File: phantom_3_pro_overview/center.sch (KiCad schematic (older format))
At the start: 0 parts

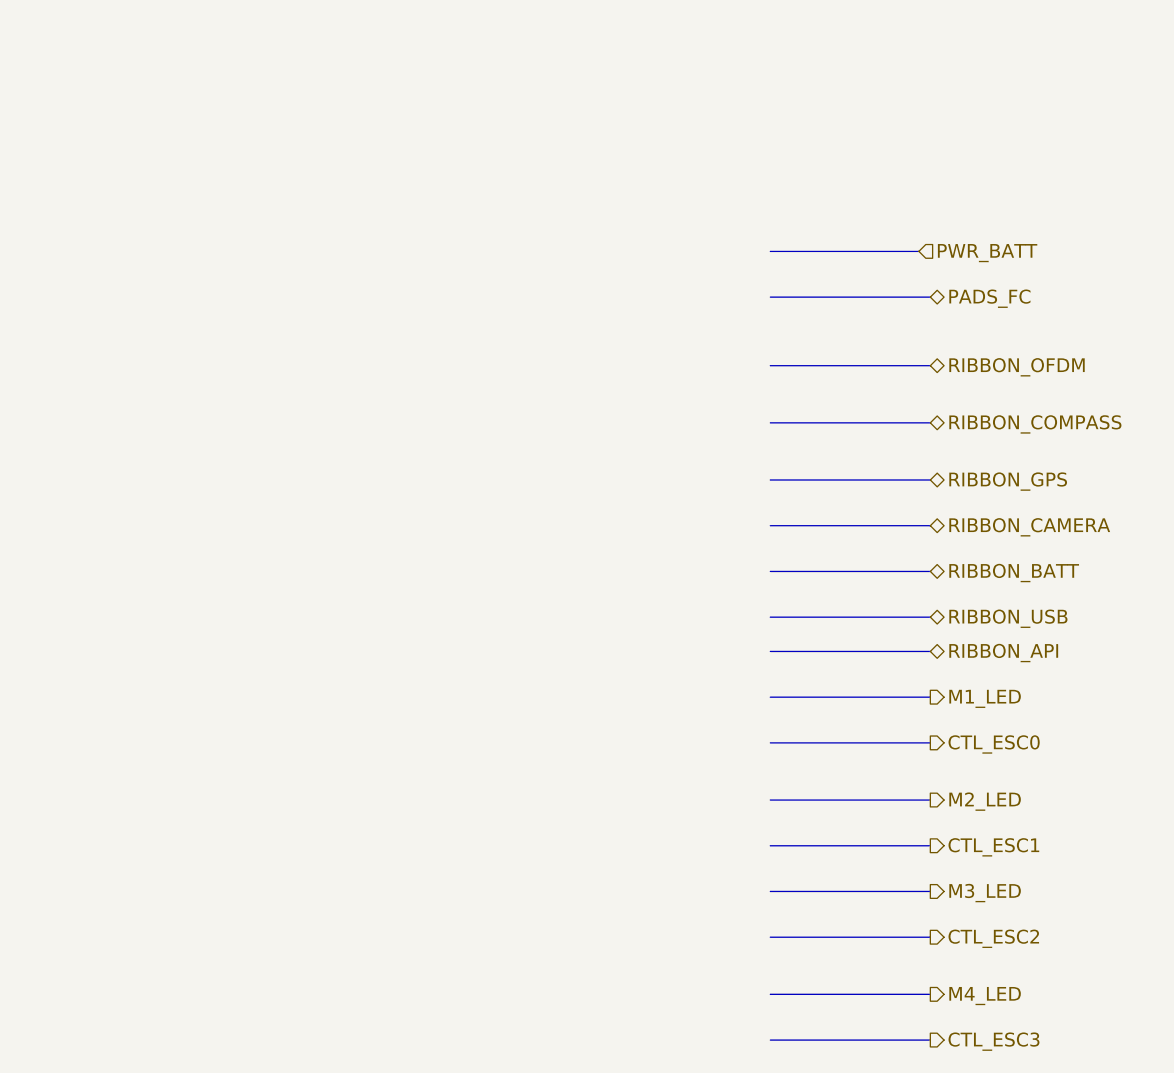
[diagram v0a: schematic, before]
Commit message: Overview: Conceptual schematics of some components.
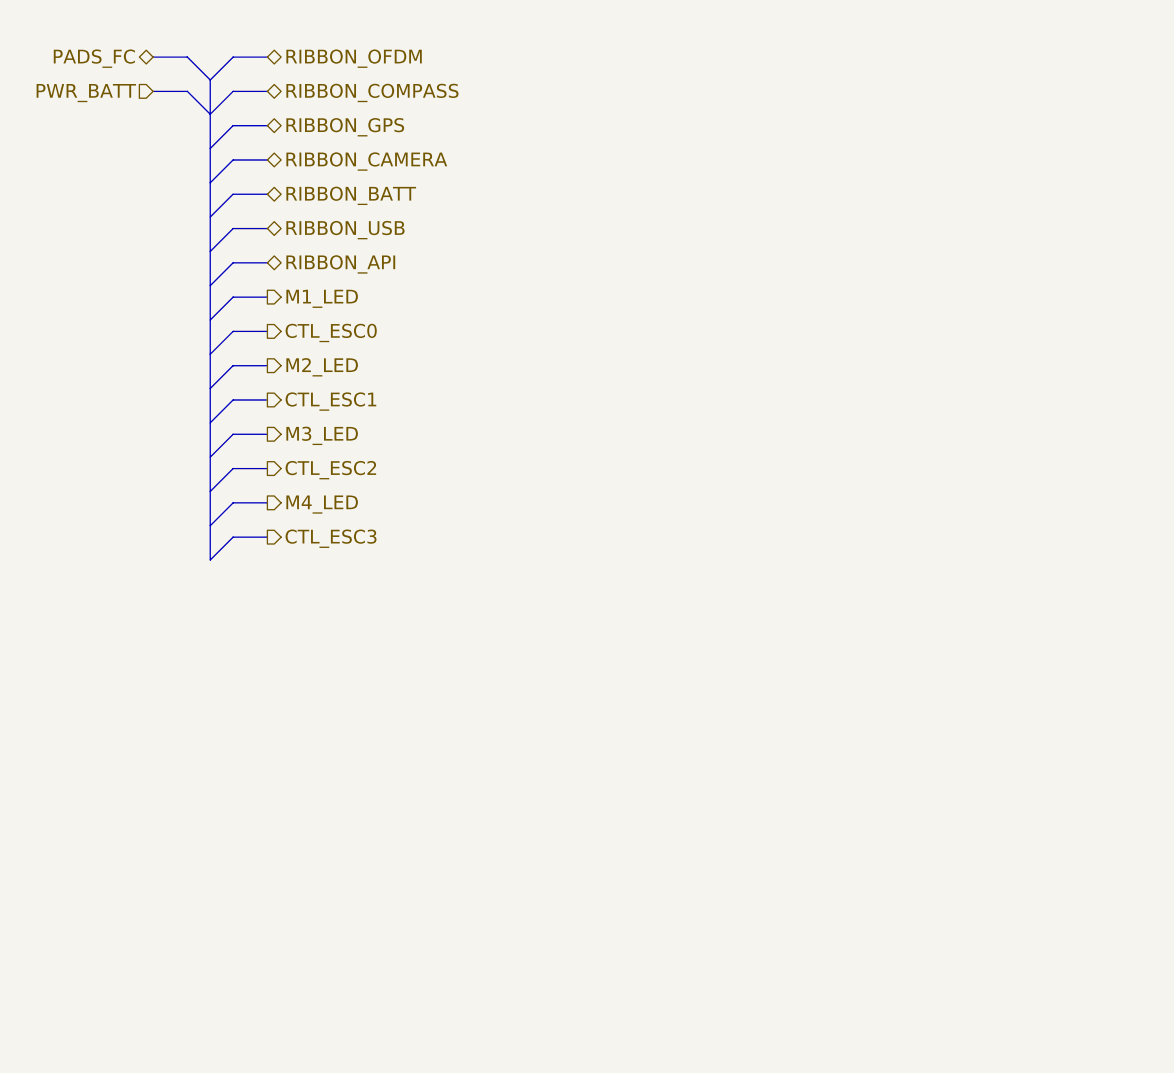
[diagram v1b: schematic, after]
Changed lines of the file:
@@
 LIBS:valves
 LIBS:motors
+LIBS:ic_dil_generic
+LIBS:sensors
+LIBS:u-blox
+LIBS:amplifiers
 LIBS:phantom_3_pro_overview-cache
 EELAYER 25 0
 EELAYER END
-$Descr A4 11693 8268
+$Descr User 5354 4725
 encoding utf-8
-Sheet 18 23
-Title ""
+Sheet 14 23
+Title "Overview of the Phantom 3 Pro Center part of MB"
 Date ""
 Rev ""
 Comp ""
-Comment1 ""
+Comment1 "This schematic does not aim to be electrically correct, it is conceptual."
 Comment2 ""
 Comment3 ""
 Comment4 ""
 $EndDescr
+Text HLabel 1050 700  0    60   BiDi ~ 0
+PADS_FC
+Text HLabel 1550 700  2    60   BiDi ~ 0
+RIBBON_OFDM
+Text HLabel 1550 850  2    60   BiDi ~ 0
+RIBBON_COMPASS
+Text HLabel 1550 1000 2    60   BiDi ~ 0
+RIBBON_GPS
+Text HLabel 1550 1150 2    60   BiDi ~ 0
+RIBBON_CAMERA
+Text HLabel 1550 1300 2    60   BiDi ~ 0
+RIBBON_BATT
+Text HLabel 1550 1450 2    60   BiDi ~ 0
+RIBBON_USB
+Text HLabel 1550 1600 2    60   BiDi ~ 0
+RIBBON_API
+Text HLabel 1550 1750 2    60   Output ~ 0
+M1_LED
+Text HLabel 1550 1900 2    60   Output ~ 0
+CTL_ESC0
+Text HLabel 1050 850  0    60   Input ~ 0
+PWR_BATT
+Text HLabel 1550 2050 2    60   Output ~ 0
+M2_LED
+Text HLabel 1550 2200 2    60   Output ~ 0
+CTL_ESC1
+Text HLabel 1550 2350 2    60   Output ~ 0
+M3_LED
+Text HLabel 1550 2500 2    60   Output ~ 0
+CTL_ESC2
+Text HLabel 1550 2650 2    60   Output ~ 0
+M4_LED
+Text HLabel 1550 2800 2    60   Output ~ 0
+CTL_ESC3
+Entry Bus Bus
+	1200 700  1300 800
 Wire Bus Line
-	3750 1750 4450 1750
-Text HLabel 4450 1750 2    60   BiDi ~ 0
-PADS_FC
+	1050 700  1200 700
 Wire Bus Line
-	3750 2050 4450 2050
+	1050 850  1200 850
+Entry Bus Bus
+	1200 850  1300 950
+Entry Bus Bus
+	1300 800  1400 700
+Entry Bus Bus
+	1300 950  1400 850
 Wire Bus Line
-	3750 2300 4450 2300
+	1400 700  1550 700
 Wire Bus Line
-	3750 2550 4450 2550
-Text HLabel 4450 2050 2    60   BiDi ~ 0
-RIBBON_OFDM
-Text HLabel 4450 2300 2    60   BiDi ~ 0
-RIBBON_COMPASS
-Text HLabel 4450 2550 2    60   BiDi ~ 0
-RIBBON_GPS
+	1400 850  1550 850
+Entry Bus Bus
+	1300 1100 1400 1000
+Entry Bus Bus
+	1300 1250 1400 1150
 Wire Bus Line
-	3750 2750 4450 2750
+	1400 1000 1550 1000
 Wire Bus Line
-	3750 2950 4450 2950
+	1400 1150 1550 1150
+Entry Bus Bus
+	1300 1400 1400 1300
+Entry Bus Bus
+	1300 1550 1400 1450
 Wire Bus Line
-	3750 3150 4450 3150
-Text HLabel 4450 2750 2    60   BiDi ~ 0
-RIBBON_CAMERA
-Text HLabel 4450 2950 2    60   BiDi ~ 0
-RIBBON_BATT
+	1400 1300 1550 1300
 Wire Bus Line
-	3750 3300 4450 3300
+	1400 1450 1550 1450
+Entry Bus Bus
+	1300 1700 1400 1600
+Entry Bus Bus
+	1300 1850 1400 1750
 Wire Bus Line
-	3750 3500 4450 3500
+	1400 1600 1550 1600
 Wire Bus Line
-	3750 3700 4450 3700
-Text HLabel 4450 3150 2    60   BiDi ~ 0
-RIBBON_USB
-Text HLabel 4450 3300 2    60   BiDi ~ 0
-RIBBON_API
-Text HLabel 4450 3500 2    60   Output ~ 0
-M1_LED
-Text HLabel 4450 3700 2    60   Output ~ 0
-CTL_ESC0
+	1400 1750 1550 1750
+Entry Bus Bus
+	1300 2000 1400 1900
+Entry Bus Bus
+	1300 2150 1400 2050
 Wire Bus Line
-	3750 1550 4400 1550
-Text HLabel 4400 1550 2    60   Input ~ 0
-PWR_BATT
+	1400 1900 1550 1900
 Wire Bus Line
-	3750 3950 4450 3950
+	1400 2050 1550 2050
+Entry Bus Bus
+	1300 2300 1400 2200
+Entry Bus Bus
+	1300 2450 1400 2350
 Wire Bus Line
-	3750 4150 4450 4150
-Text HLabel 4450 3950 2    60   Output ~ 0
-M2_LED
-Text HLabel 4450 4150 2    60   Output ~ 0
-CTL_ESC1
+	1400 2200 1550 2200
 Wire Bus Line
-	3750 4350 4450 4350
+	1400 2350 1550 2350
+Entry Bus Bus
+	1300 2600 1400 2500
+Entry Bus Bus
+	1300 2750 1400 2650
 Wire Bus Line
-	3750 4550 4450 4550
-Text HLabel 4450 4350 2    60   Output ~ 0
-M3_LED
-Text HLabel 4450 4550 2    60   Output ~ 0
-CTL_ESC2
+	1400 2500 1550 2500
 Wire Bus Line
-	3750 4800 4450 4800
+	1400 2650 1550 2650
+Entry Bus Bus
+	1300 2900 1400 2800
 Wire Bus Line
-	3750 5000 4450 5000
-Text HLabel 4450 4800 2    60   Output ~ 0
-M4_LED
-Text HLabel 4450 5000 2    60   Output ~ 0
-CTL_ESC3
+	1400 2800 1550 2800
+Wire Bus Line
+	1300 800  1300 2900
 $EndSCHEMATC

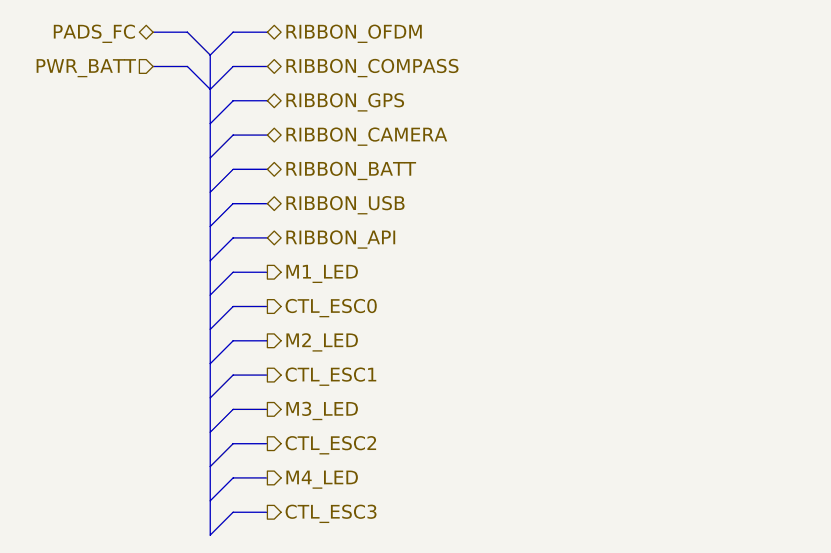
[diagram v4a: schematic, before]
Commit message: Overview: Added power converters.
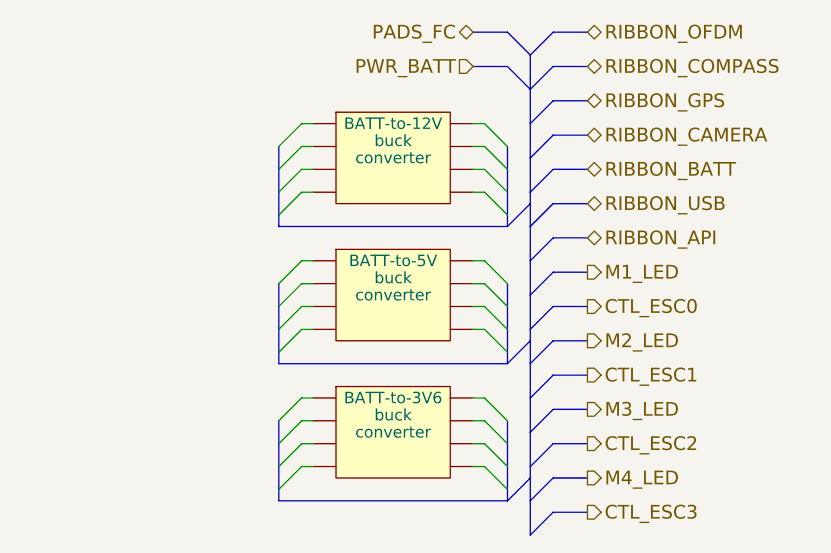
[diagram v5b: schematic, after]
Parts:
- added U?: BATT-to-3V6, buck, symbol IC_DIL8
- added U?: BATT-to-12V, buck, symbol IC_DIL8
- added U?: BATT-to-5V, buck, symbol IC_DIL8

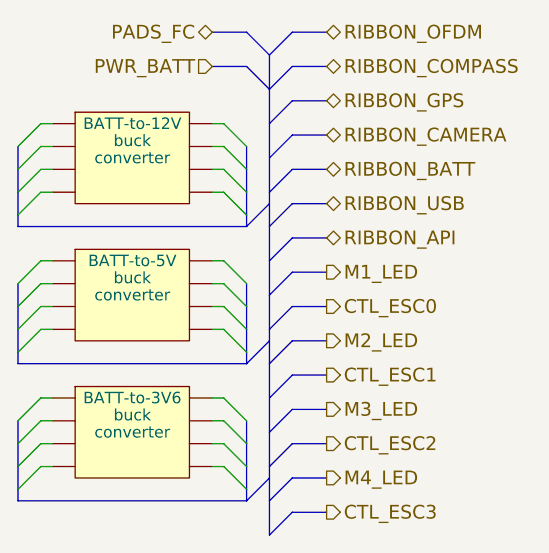
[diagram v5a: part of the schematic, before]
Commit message: Overview: Drawn the camera encoder block.
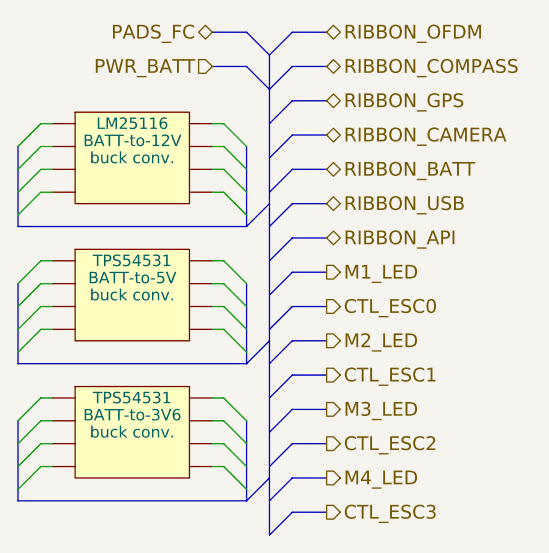
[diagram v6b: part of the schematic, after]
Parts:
- U?: value BATT-to-3V6 -> TPS54531; footprint buck -> BATT-to-3V6
- U?: value BATT-to-12V -> LM25116; footprint buck -> BATT-to-12V
- U?: value BATT-to-5V -> TPS54531; footprint buck -> BATT-to-5V
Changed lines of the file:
@@
 	1600 2700 1700 2600
 Wire Bus Line
-	1600 1200 1600 1300
+	1600 1200 1600 1550
 Wire Bus Line
-	1600 1300 1600 1400
+	2600 1200 2600 1550
 Wire Bus Line
-	1600 1400 1600 1500
+	1600 1800 1600 2150
 Wire Bus Line
-	1600 1500 1600 1550
+	2600 2150 1600 2150
 Wire Bus Line
-	2600 1550 2600 1500
+	2600 1800 2600 2150
 Wire Bus Line
-	2600 1500 2600 1400
+	1600 2400 1600 2750
 Wire Bus Line
-	2600 1400 2600 1300
+	2600 2750 1600 2750
 Wire Bus Line
-	2600 1300 2600 1200
-Wire Bus Line
-	1600 1800 1600 1900
-Wire Bus Line
-	1600 1900 1600 2000
-Wire Bus Line
-	1600 2000 1600 2100
-Wire Bus Line
-	1600 2100 1600 2150
-Wire Bus Line
-	1600 2150 2600 2150
-Wire Bus Line
-	2600 2150 2600 2100
-Wire Bus Line
-	2600 2100 2600 2000
-Wire Bus Line
-	2600 2000 2600 1900
-Wire Bus Line
-	2600 1900 2600 1800
-Wire Bus Line
-	1600 2400 1600 2500
-Wire Bus Line
-	1600 2500 1600 2600
-Wire Bus Line
-	1600 2600 1600 2700
-Wire Bus Line
-	1600 2700 1600 2750
-Wire Bus Line
-	1600 2750 2600 2750
-Wire Bus Line
-	2600 2750 2600 2700
-Wire Bus Line
-	2600 2700 2600 2600
-Wire Bus Line
-	2600 2600 2600 2500
-Wire Bus Line
-	2600 2500 2600 2400
+	2600 2400 2600 2750
 Entry Bus Bus
 	2600 1550 2700 1450
@@
 P 2100 2450
 F 0 "U?" H 2100 2300 50  0001 C CNN
-F 1 "BATT-to-3V6" H 2100 2600 50  0000 C CNN
-F 2 "buck" H 2100 2525 50  0000 C CNN
-F 3 "converter" H 2100 2450 50  0000 C CNN
+F 1 "TPS54531" H 2100 2600 50  0000 C CNN
+F 2 "BATT-to-3V6" H 2100 2525 50  0000 C CNN
+F 3 "buck conv." H 2100 2450 50  0000 C CNN
 	1    2100 2450
 	1    0    0    -1
@@
 P 2100 1250
 F 0 "U?" H 2100 1100 50  0001 C CNN
-F 1 "BATT-to-12V" H 2100 1400 50  0000 C CNN
-F 2 "buck" H 2100 1325 50  0000 C CNN
-F 3 "converter" H 2100 1250 50  0000 C CNN
+F 1 "LM25116" H 2100 1400 50  0000 C CNN
+F 2 "BATT-to-12V" H 2100 1325 50  0000 C CNN
+F 3 "buck conv." H 2100 1250 50  0000 C CNN
 	1    2100 1250
 	1    0    0    -1
@@
 P 2100 1850
 F 0 "U?" H 2100 1700 50  0001 C CNN
-F 1 "BATT-to-5V" H 2100 2000 50  0000 C CNN
-F 2 "buck" H 2100 1925 50  0000 C CNN
-F 3 "converter" H 2100 1850 50  0000 C CNN
+F 1 "TPS54531" H 2100 2000 50  0000 C CNN
+F 2 "BATT-to-5V" H 2100 1925 50  0000 C CNN
+F 3 "buck conv." H 2100 1850 50  0000 C CNN
 	1    2100 1850
 	1    0    0    -1
 $EndComp
 Wire Bus Line
-	1600 1550 2600 1550
+	2600 1550 1600 1550
 Wire Wire Line
 	1700 2300 1750 2300
@@
 	2500 1400 2450 1400
 Wire Bus Line
-	2700 800  2700 800
-Wire Bus Line
-	2700 800  2700 900
-Wire Bus Line
-	2700 900  2700 950
-Wire Bus Line
-	2700 950  2700 1100
-Wire Bus Line
-	2700 1100 2700 1250
-Wire Bus Line
-	2700 1250 2700 1400
-Wire Bus Line
-	2700 1400 2700 1450
-Wire Bus Line
-	2700 1450 2700 1550
-Wire Bus Line
-	2700 1550 2700 1700
-Wire Bus Line
-	2700 1700 2700 1850
-Wire Bus Line
-	2700 1850 2700 2000
-Wire Bus Line
-	2700 2000 2700 2050
-Wire Bus Line
-	2700 2050 2700 2150
-Wire Bus Line
-	2700 2150 2700 2300
-Wire Bus Line
-	2700 2300 2700 2450
-Wire Bus Line
-	2700 2450 2700 2600
-Wire Bus Line
-	2700 2600 2700 2650
-Wire Bus Line
-	2700 2650 2700 2750
-Wire Bus Line
-	2700 2750 2700 2900
+	2700 800  2700 2900
 $EndSCHEMATC
